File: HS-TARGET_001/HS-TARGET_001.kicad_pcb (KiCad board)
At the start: 2 copper layers, 85 x 85 mm, 43 parts, among them J1 5V_Serial, J2 i2c, J3 ICSP, J4 PROG, J5 dry_cell, Q1 Q_NMOS_GDS, Q2 Q_NMOS_GDS, Q3 Q_NMOS_GDS, SW1 RESET, SW2 SW_DIP_x04, U1 TSOP59540TR1, U2 ATmega328P-PU, U3 DFPLAYER_MINI, U4 TWELITE_DIP, U5 R-781.8-1.0, U6 AE-XCL102D503CR-G, Y1 Crystal

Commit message: ・HS-TARGET001基盤修正 ・HS-TAGLED001 開始
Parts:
- removed JP3: Jumper, Connector_PinHeader_2.54mm:PinHeader_1x02_P2.54mm_Vertical
- C3, D2, U1: moved to B.Cu
- R1, R10, R7, R8, R9: footprint Resistor_THT:R_Axial_DIN0204_L3.6mm_D1.6mm_P7.62mm_Horizontal -> Resistor_SMD:R_1206_3216Metric; moved to B.Cu
- R2, R3, R4, R5, R6: footprint Resistor_THT:R_Axial_DIN0204_L3.6mm_D1.6mm_P7.62mm_Horizontal -> Resistor_SMD:R_1206_3216Metric
- SW1: footprint Button_Switch_THT:SW_TH_Tactile_Omron_B3F-10xx -> digikey-footprints:Switch_Tactile_THT_6x6mm
- moved J5 140.3 mm to (77.6, 120.2)
- moved LS1 119.6 mm to (70.0, 112.1), turned to 90 degrees
- moved J2 119.3 mm to (77.6, 114.6), turned to 180 degrees
- moved C3 119.3 mm to (79.6, 77.5), turned to 270 degrees
- moved F1 115.7 mm to (82.2, 122.7)
- moved R3 113.2 mm to (72.5, 117.1)
- moved R8 105.0 mm to (100.5, 128.3), turned to 270 degrees
- moved R7 103.0 mm to (79.6, 70.9), turned to 270 degrees
- moved R4 99.4 mm to (72.5, 120.2)
- moved R9 92.1 mm to (106.5, 128.3), turned to 270 degrees
- moved R1 84.0 mm to (76.1, 93.3), turned to 270 degrees
- moved R5 83.3 mm to (104.5, 115.1), turned to 90 degrees
- moved JP4 82.9 mm to (125.3, 65.3), turned to 180 degrees
- moved C2 77.0 mm to (104.5, 90.7), turned to 180 degrees
- moved C1 75.9 mm to (102.0, 61.3), turned to 180 degrees
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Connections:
- Q1 pad 2: Net-(Q1-Pad2) -> GND
- Q1 pad 3: GND -> Net-(Q1-Pad2)
- Q2 pad 2: Net-(Q2-Pad2) -> GND
- Q2 pad 3: GND -> Net-(Q2-Pad2)
- Q3 pad 2: Net-(Q3-Pad2) -> GND
- Q3 pad 3: GND -> Net-(Q3-Pad2)
- U6 pad 6: Net-(JP3-Pad1) -> Net-(C4-Pad1)
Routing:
- net GND: track 0.00 -> 272.4 mm
- net +5V: track 0.00 -> 169.5 mm
- net RXOUT: track 0.00 -> 80.7 mm
- net +3.3V: track 0.00 -> 77.0 mm
- net TXOUT: track 0.00 -> 76.9 mm
- net Net-(J4-Pad2): track 0.00 -> 66.2 mm
- net Net-(J2-Pad2): track 0.00 -> 62.0 mm
- net Net-(R5-Pad2): track 0.00 -> 60.0 mm
- net LED_G: track 0.00 -> 59.9 mm
- net Net-(J2-Pad1): track 0.00 -> 59.5 mm
- net LED_R: track 0.00 -> 58.7 mm
- net LED_B: track 0.00 -> 56.7 mm
- net Net-(C4-Pad1): track 0.00 -> 54.5 mm
- net RX_J: track 0.00 -> 53.5 mm
- net Net-(U2-Pad4): track 0.00 -> 46.7 mm
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- added copper zone on B.Cu, net GND
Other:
- outline, holes or cut-outs redrawn

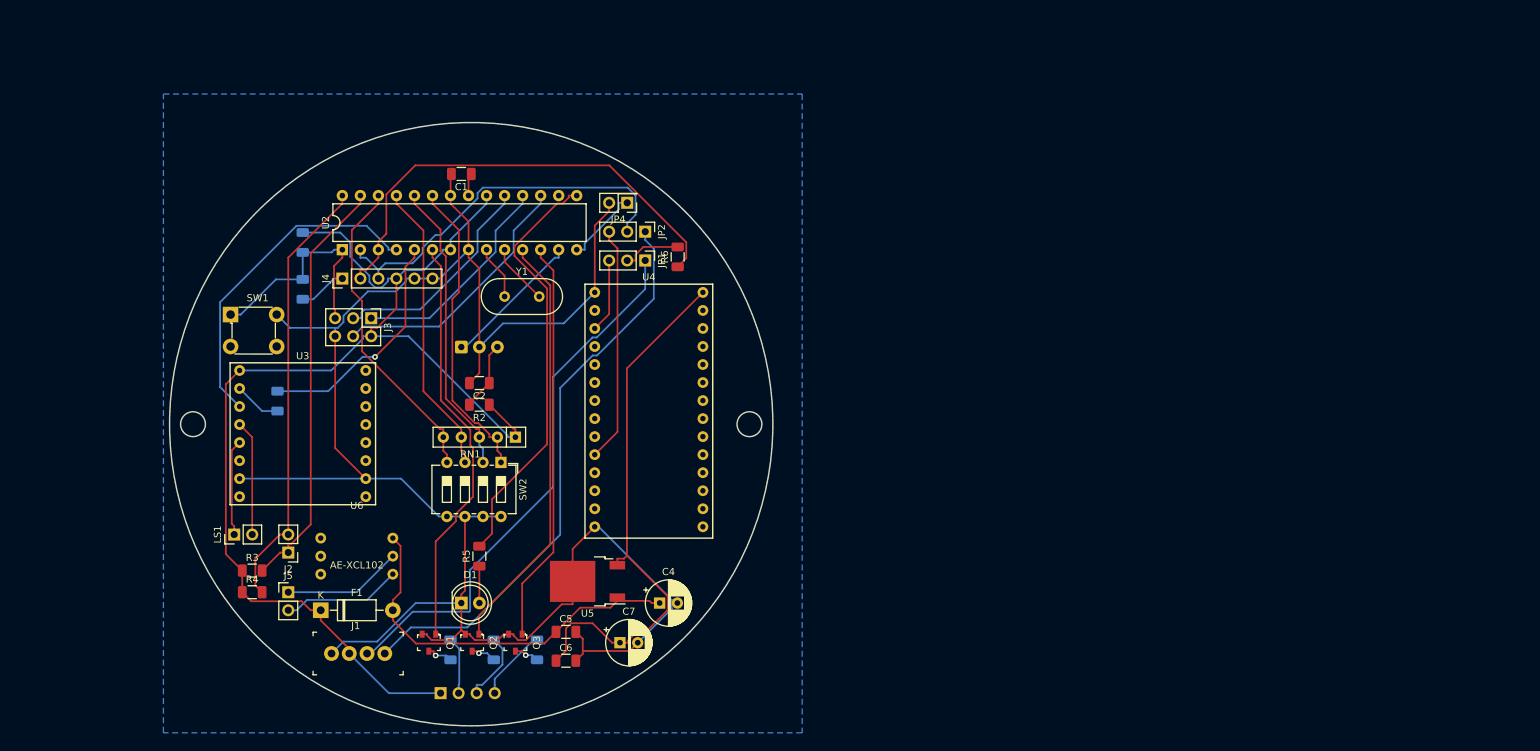
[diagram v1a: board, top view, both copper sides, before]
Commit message: ・HS-TAGLED更新
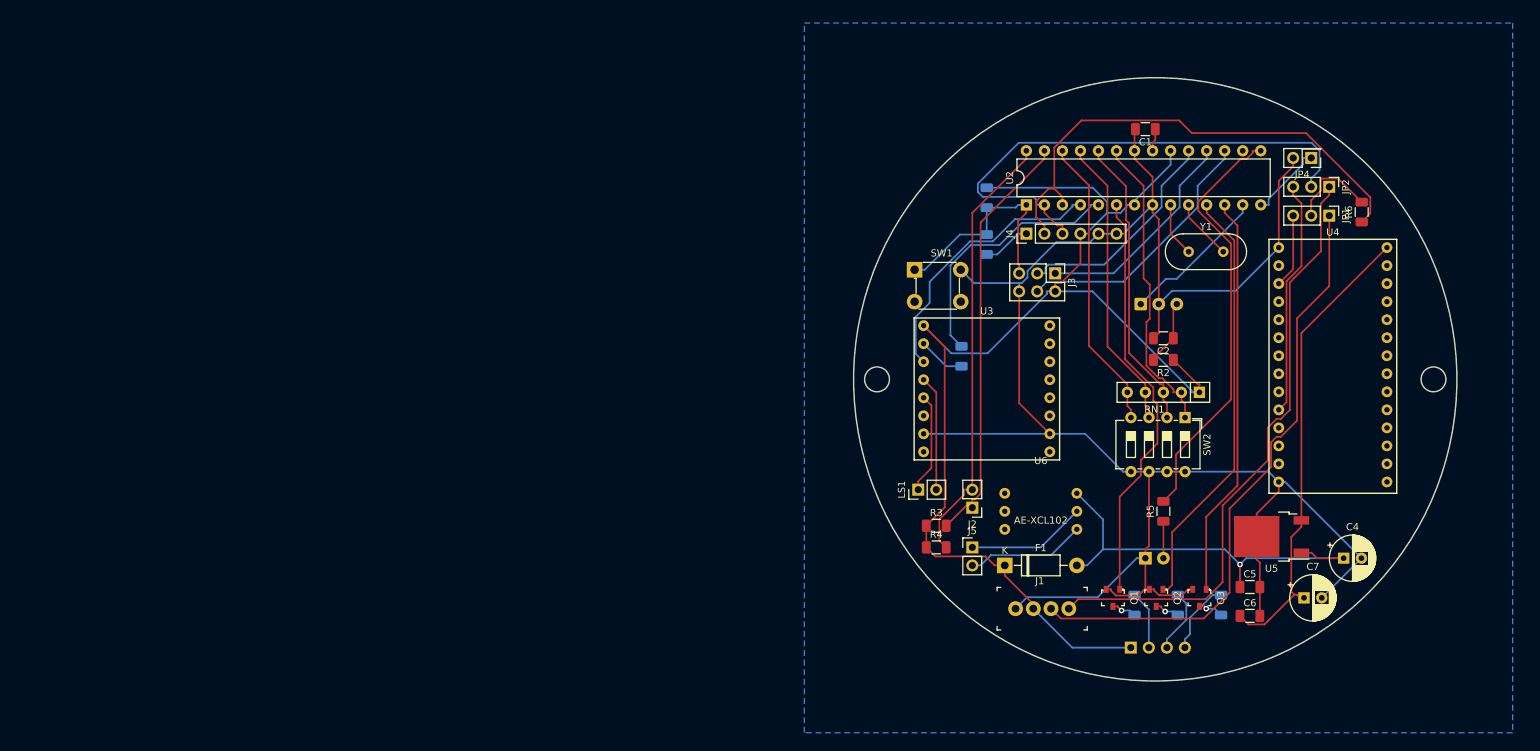
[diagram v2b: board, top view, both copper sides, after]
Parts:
- D1: moved to B.Cu
- moved D2 97.5 mm to (196.3, 128.0)
- moved C1 96.6 mm to (198.4, 54.9)
- moved JP4 96.6 mm to (221.7, 59.0)
- moved R6 96.6 mm to (228.8, 66.6)
- moved RN1 96.6 mm to (206.0, 92.0)
- moved SW2 96.6 mm to (203.9, 95.6)
- moved U4 96.6 mm to (224.8, 88.5)
- moved Y1 96.6 mm to (204.4, 72.2)
- moved C2 96.6 mm to (200.9, 84.4)
- moved JP1 96.6 mm to (224.3, 67.1)
- moved JP2 96.6 mm to (224.3, 63.1)
- moved R2 96.6 mm to (200.9, 87.5)
- moved C4 96.6 mm to (226.3, 115.4)
- moved C5 96.6 mm to (213.1, 119.5)
- moved C6 96.6 mm to (213.1, 123.5)
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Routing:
- net RX_J: track 53.5 -> 73.8 mm
- net +3.3V: track 77.0 -> 66.1 mm
- net TXOUT: track 76.9 -> 86.5 mm
- net Net-(U2-Pad4): track 46.7 -> 38.4 mm
- net +5V: track 169.5 -> 175.0 mm
- net Net-(J4-Pad2): track 66.2 -> 71.5 mm
- net RXOUT: track 80.7 -> 85.5 mm
- net TX_J: track 8.38 -> 12.9 mm
- net Net-(C4-Pad1): track 54.5 -> 58.7 mm, vias 0 -> 1
- net Net-(R1-Pad1): track 33.2 -> 36.6 mm, vias 1 -> 0
- net ID_SW4: track 45.0 -> 41.6 mm
- net GND: track 272.4 -> 269.9 mm
- net Net-(D2-Pad3): track 9.97 -> 9.03 mm
- net IRsen: track 20.1 -> 20.8 mm
- net Net-(LS1-Pad1): track 13.6 -> 14.2 mm
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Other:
- outline, holes or cut-outs redrawn

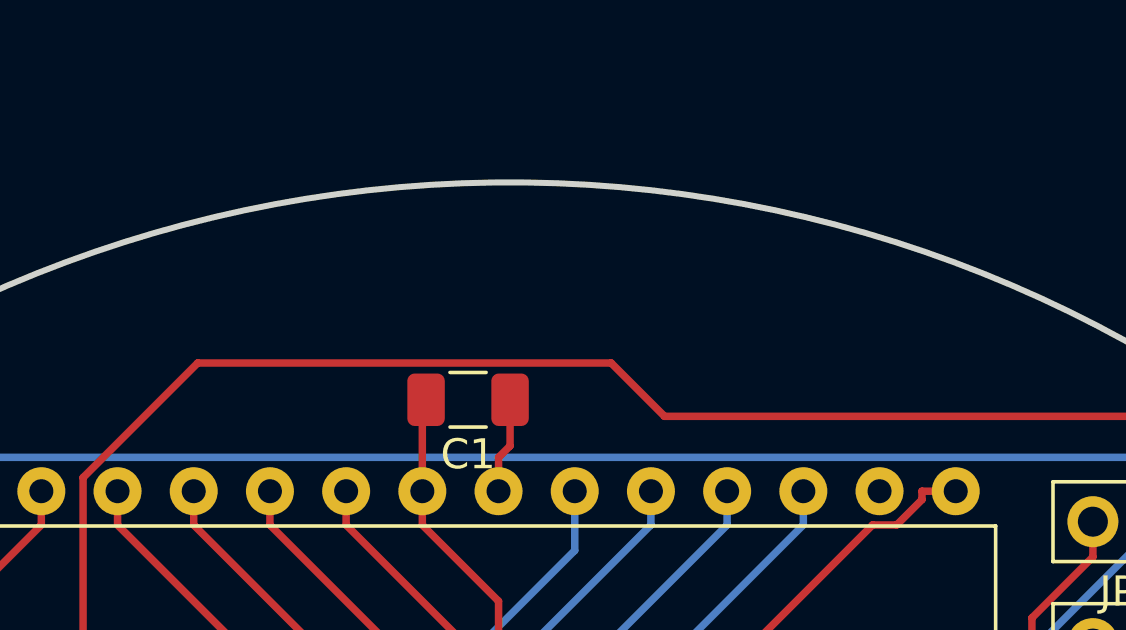
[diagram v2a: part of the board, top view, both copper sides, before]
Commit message: ・各基盤修正
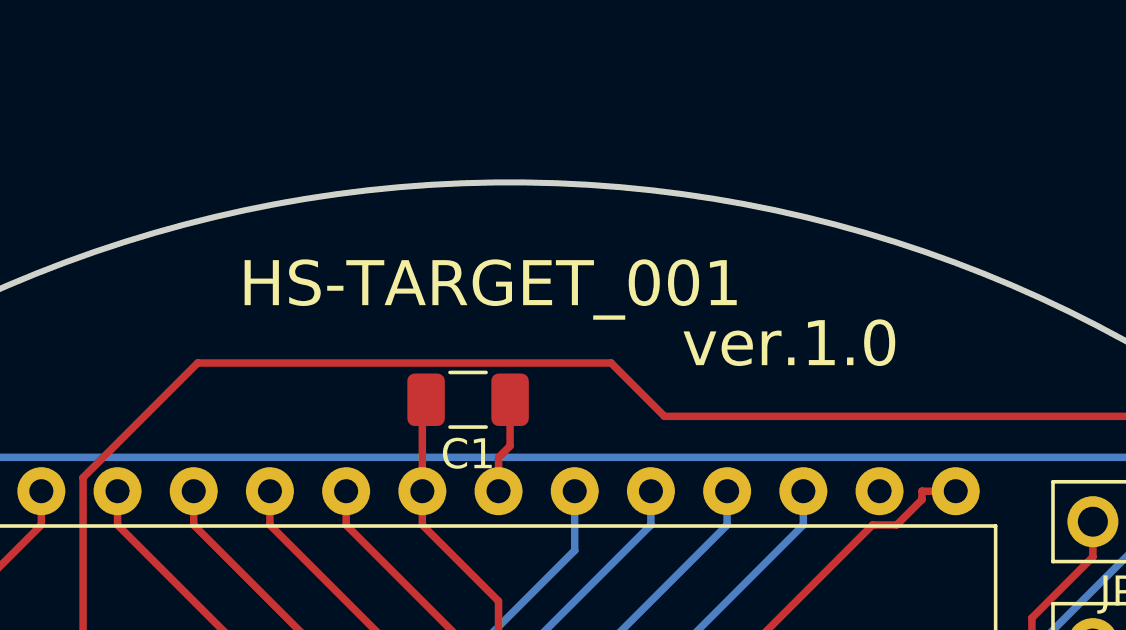
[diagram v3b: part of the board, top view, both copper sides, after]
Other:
- board text added: "HS-TARGET_001"
- board text added: "ver.1.0"
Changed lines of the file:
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@@
-(kicad_pcb (version 20171130) (host pcbnew "(5.1.2-1)-1")
+(kicad_pcb (version 20171130) (host pcbnew "(5.1.2)-2")
   (general
     (thickness 1.6)
-    (drawings 5)
+    (drawings 7)
     (tracks 426)
     (zones 0)
@@
     (pad_to_mask_clearance 0.051)
     (solder_mask_min_width 0.25)
-    (aux_axis_origin 0 0)
-    (grid_origin 200.1 90.1)
-    (visible_elements 7FFFF7FF)
+    (aux_axis_origin 150.1 140.1)
+    (grid_origin 150.1 140.1)
+    (visible_elements 7FFFFFFF)
     (pcbplotparams
-      (layerselection 0x010fc_ffffffff)
-      (usegerberextensions false)
+      (layerselection 0x090fc_ffffffff)
+      (usegerberextensions true)
       (usegerberattributes false)
       (usegerberadvancedattributes false)
@@
       (plotinvisibletext false)
       (padsonsilk false)
-      (subtractmaskfromsilk false)
+      (subtractmaskfromsilk true)
       (outputformat 1)
       (mirror false)
-      (drillshape 1)
+      (drillshape 0)
       (scaleselection 1)
-      (outputdirectory ""))
+      (outputdirectory "C:/Users/YUUTA ISHII/Desktop/HS-TARGET001/"))
   )
   (net 0 "")
@@
     (pad 3 thru_hole circle (at 0 4.5) (size 2.2 2.2) (drill 1.2) (layers *.Cu *.Mask))
   )
+  (gr_text ver.1.0 (at 209.1 53.1) (layer F.SilkS)
+    (effects (font (size 1.5 1.5) (thickness 0.3)))
+  )
+  (gr_text HS-TARGET_001 (at 199.1 51.1) (layer F.SilkS)
+    (effects (font (size 1.5 1.5) (thickness 0.3)))
+  )
   (gr_line (start 200.2 40.2) (end 200.1 150.3) (layer Eco1.User) (width 0.15))

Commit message: ・修正
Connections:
- SW1 pad 2: GND -> (no net)
- SW1 pad 4: (no net) -> GND
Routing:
- net GND: track 269.9 -> 271.3 mm
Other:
- board text added: "ver.1.1"
- board text removed: "ver.1.0"
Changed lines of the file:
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@@
-(kicad_pcb (version 20171130) (host pcbnew "(5.1.2)-2")
+(kicad_pcb (version 20171130) (host pcbnew "(5.1.2-1)-1")
   (general
     (thickness 1.6)
     (drawings 7)
-    (tracks 426)
+    (tracks 427)
     (zones 0)
     (modules 42)
@@
     (mod_text_size 1 1)
     (mod_text_width 0.15)
-    (pad_size 1 0.7)
-    (pad_drill 0)
+    (pad_size 2.2 2.2)
+    (pad_drill 1.2)
     (pad_to_mask_clearance 0.051)
     (solder_mask_min_width 0.25)
@@
     (pad 1 thru_hole rect (at 0 0) (size 2.2 2.2) (drill 1.2) (layers *.Cu *.Mask)
       (net 4 "Net-(C3-Pad1)"))
-    (pad 2 thru_hole circle (at 6.5 0) (size 2.2 2.2) (drill 1.2) (layers *.Cu *.Mask)
+    (pad 2 thru_hole circle (at 6.5 0) (size 2.2 2.2) (drill 1.2) (layers *.Cu *.Mask))
+    (pad 4 thru_hole circle (at 6.5 4.5) (size 2.2 2.2) (drill 1.2) (layers *.Cu *.Mask)
       (net 2 GND))
-    (pad 4 thru_hole circle (at 6.5 4.5) (size 2.2 2.2) (drill 1.2) (layers *.Cu *.Mask))
     (pad 3 thru_hole circle (at 0 4.5) (size 2.2 2.2) (drill 1.2) (layers *.Cu *.Mask))
   )
-  (gr_text ver.1.0 (at 209.1 53.1) (layer F.SilkS)
+  (gr_text ver.1.1 (at 209.1 53.1) (layer F.SilkS)
     (effects (font (size 1.5 1.5) (thickness 0.3)))
   )
@@
   (segment (start 195.1947 103.208) (end 189.8607 97.874) (width 0.25) (layer B.Cu) (net 2))
   (segment (start 189.8607 97.874) (end 184.89 97.874) (width 0.25) (layer B.Cu) (net 2))
-  (segment (start 172.34 74.76) (end 174.2127 76.6327) (width 0.25) (layer B.Cu) (net 2))
-  (segment (start 174.2127 76.6327) (end 180.572 76.6327) (width 0.25) (layer B.Cu) (net 2))
   (segment (start 217.148 104.656) (end 218.048 104.656) (width 0.25) (layer B.Cu) (net 2))
   (segment (start 218.048 104.656) (end 228.792 115.4) (width 0.25) (layer B.Cu) (net 2))
@@
   (segment (start 217.148 62.2193) (end 219.18 60.1873) (width 0.25) (layer F.Cu) (net 2))
   (segment (start 214.032 112.352) (end 214.032 115.5773) (width 0.25) (layer F.Cu) (net 2))
+  (segment (start 172.34 77.474) (end 172.34 79.26) (width 0.25) (layer B.Cu) (net 2))
+  (segment (start 173.1813 76.6327) (end 172.34 77.474) (width 0.25) (layer B.Cu) (net 2))
+  (segment (start 180.572 76.6327) (end 173.1813 76.6327) (width 0.25) (layer B.Cu) (net 2))
   (segment (start 202.292 84.412) (end 199.492 87.212) (width 0.25) (layer F.Cu) (net 3))
   (segment (start 199.492 87.212) (end 199.492 87.46) (width 0.25) (layer F.Cu) (net 3))
@@
     (polygon
       (pts
-        (xy 150.3 40) (xy 250.1 40) (xy 250.1 140) (xy 150.3 140)
+        (xy 150.1 38.754) (xy 251.954 38.754) (xy 251.954 140.608) (xy 150.1 140.608)
       )
     )
